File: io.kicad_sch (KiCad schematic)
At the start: 23 parts, among them SW1 KMR221GLFS, SW2 KMR221GLFS, SW3 KMR221GLFS, SW4 KMR221GLFS, SW5 KMR221GLFS, SW6 KMR221GLFS, SW7 KMR221GLFS, U8 KMR241GLFS, U9 KMR241GLFS

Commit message: pcb / inital work
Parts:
- removed C23: 4.7uF/16V, 7XR, Capacitor_THT:CP_Radial_D5.0mm_P2.50mm, symbol PCM_SL_Devices:Capacitor_PO
- removed C24: 2.2uF, Capacitor_THT:C_Disc_D3.0mm_W2.0mm_P2.50mm, symbol PCM_SL_Devices:Capacitor_NP
- removed C30, C31: 0.1uF, Capacitor_THT:C_Disc_D3.0mm_W2.0mm_P2.50mm, symbol PCM_SL_Devices:Capacitor_NP
- removed C6, C7: 1uF/16V, X5R, Capacitor_THT:C_Disc_D3.0mm_W2.0mm_P2.50mm, symbol PCM_SL_Devices:Capacitor_NP
- removed C8: 1uF, Capacitor_THT:C_Disc_D3.0mm_W2.0mm_P2.50mm, symbol PCM_SL_Devices:Capacitor_NP
- removed DS1: OLED-128O064D, Display:OLED-128O064D, symbol Display_Graphic:OLED-128O064D
- removed ENC1, ENC2, ENC3: Encoder_Rotary_11mm_SPST_DShaft, 4ms_Encoder:ENC_SPST_12mm, symbol PCM_4ms_Switch:Encoder_Rotary_11mm_SPST_DShaft
- added J3: 5051102291, CON_5051102291_MOL, symbol uwu:4421
- added MT1, MT2, MT3: RIC11-22S11K5S-USMT, uwu:XDCR_RIC11-22S11K5S-USMT, symbol uwu:RIC11-22S11K5S-USMT
- added R43, R44, R45, R46: 10k, Resistor_SMD:R_0603_1608Metric, symbol PCM_Elektuur:R
- added S1, S2, S3: AYZ0102AGRLC, uwu:SW_AYZ0102AGRLC, symbol uwu:AYZ0102AGRLC
- R21: value 910k -> 20; footprint (none) -> Resistor_SMD:R_0603_1608Metric
- R26, R27: value 4.7k -> 10k; footprint (none) -> Resistor_SMD:R_0603_1608Metric
- U8, U9: footprint SWITCH_241GLFS -> uwu:SWITCH_241GLFS
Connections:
- net DISP_CS: now also J3.18 (CS)
- net DISP_DC: now also J3.16 (WR)
- net DISP_DIN: now also J3.21 (SDA); no longer R27.2 (-)
- net DISP_RES: now also J3.20 (RESET)
- net DISP_SCLK: now also J3.17 (RS); no longer R26.2 (-)
- net ENC1_A: now also R26.2 (-), MT1.A
- net ENC1_B: now also R27.2 (-), MT1.B
- net ENC1_SW1: now also MT1.D
- net ENC2_A: now also MT2.A, R43.2 (-)
- net ENC2_B: now also MT2.B, R44.2 (-)
- net ENC2_SW1: now also MT2.D
- net ENC3_A: now also MT3.A, R45.2 (-)
- net ENC3_B: now also MT3.B, R46.2 (-)
- net ENC3_SW1: now also MT3.D
- net GND: now also J3.15 (RD), J3.2 (LEDK), J3.22 (GND), J3.5 (IM0), MT1.C, MT1.SH1 (SHIELD), MT1.SH2 (SHIELD__1), MT2.C, MT2.SH1 (SHIELD), MT2.SH2 (SHIELD__1), MT3.C, MT3.SH1 (SHIELD), MT3.SH2 (SHIELD__1), S1.3, S2.3, S3.3; no longer R21.1 (+)
- net V3.3_SYS: now also R21.1 (+), J3.3 (IM2), J3.4 (IM1), J3.6 (VCI), MT1.E, MT2.E, MT3.E, R43.1 (+), R44.1 (+), R45.1 (+), R46.1 (+), S1.1, S2.1, S3.1
- net at R21.2 (-): now also J3.1 (LEDA)
- new net SWITCH_1: S1.2
- new net SWITCH_2: S2.2
- new net SWITCH_3: S3.2
- no-connect marks 6 -> 11

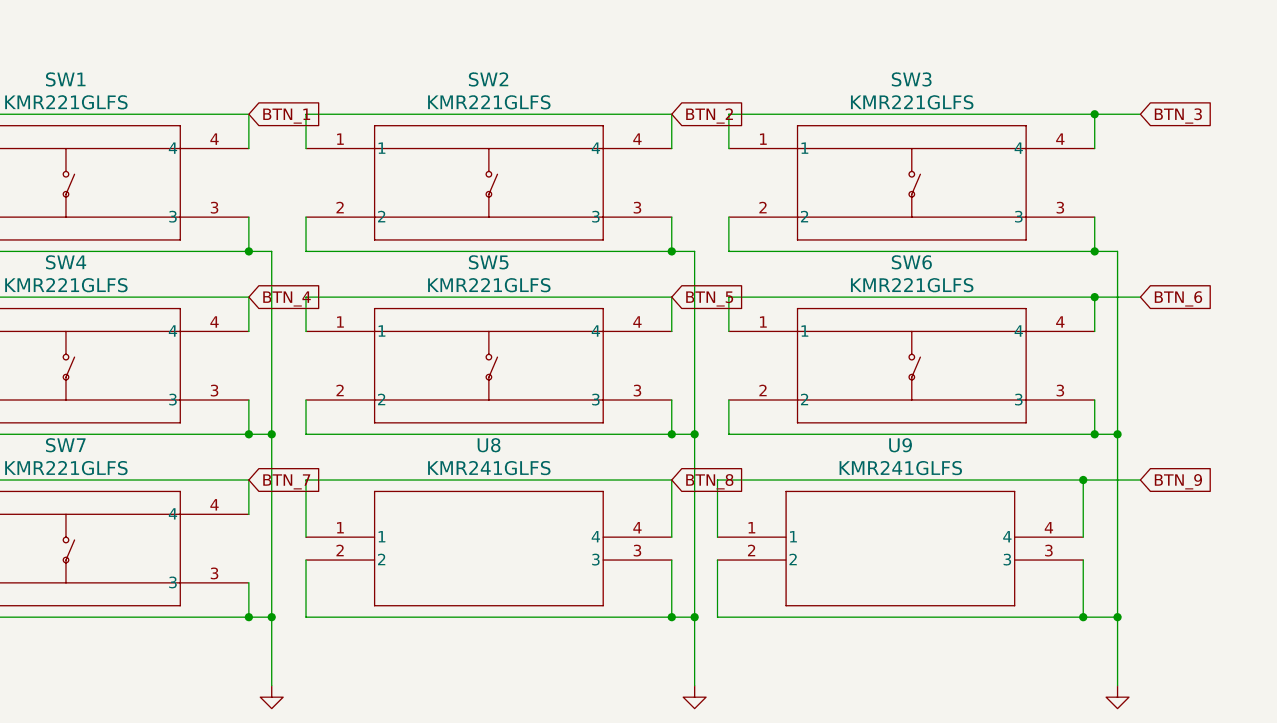
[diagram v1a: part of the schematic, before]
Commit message: all pcb elements positioned + minor schematics changes
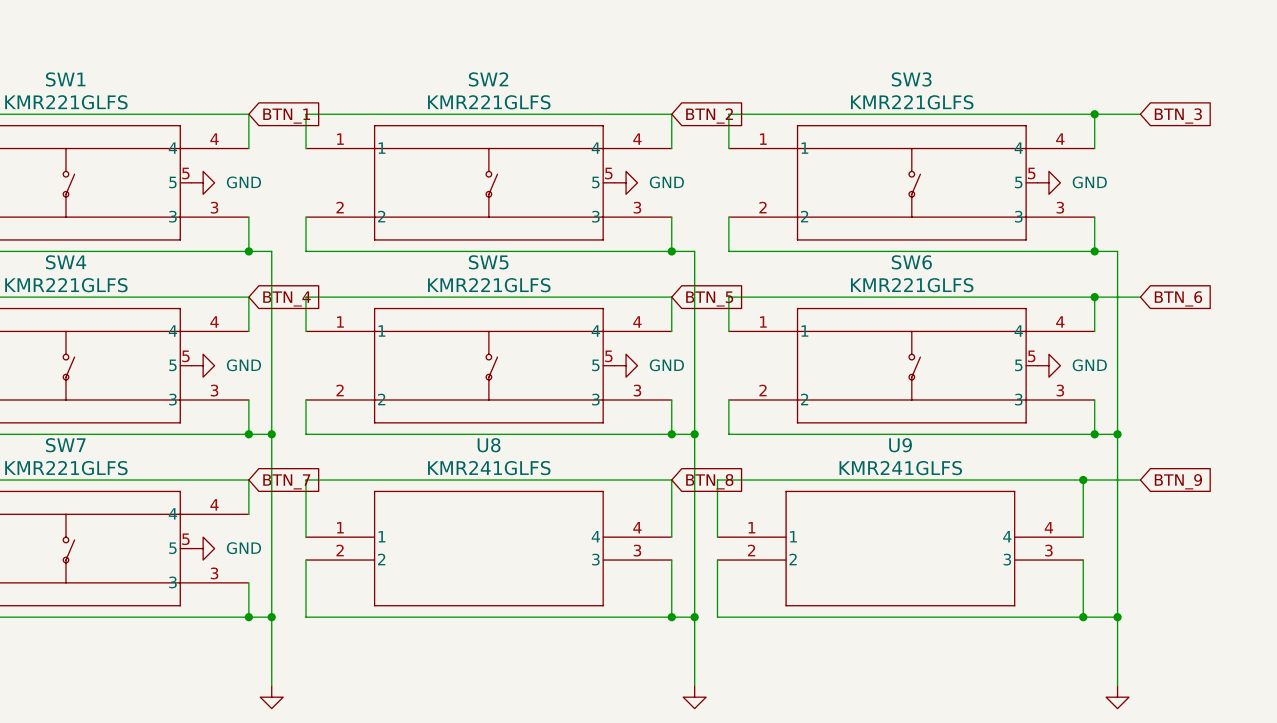
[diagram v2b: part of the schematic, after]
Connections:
- net GND: now also SW1.5, SW2.5, SW3.5, SW4.5, SW5.5, SW6.5, SW7.5
